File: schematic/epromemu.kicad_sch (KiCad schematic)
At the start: 10 parts, among them J1 EPROM Connector, U1 Teensy4.1, U2 74HC245, U3 74HC245, U4 74HC245, U5 74HC245

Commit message: v0.2 updates
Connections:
- net CE_3V3: now also U1.22 (30_CRX3); no longer U1.26 (34_RX8)
- net CE_5V: now also U2.19 (CE)
- net OE_5V: now also U5.11 (B7); no longer U2.19 (CE)
- net PGM_3V3: now also U1.20 (28_RX7), U3.11 (B7); no longer U1.25 (33_MCLK2), U5.9 (A7)
- net PGM_5V: now also U3.9 (A7); no longer U5.11 (B7)
- net OE_3V3: now reaches U1.23 (31_CTX3)
- net OE_3V3: now also U5.9 (A7)
- no-connect marks 26 -> 23
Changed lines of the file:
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@@
   (junction (at 71.12 123.19) (diameter 0) (color 0 0 0 0)
   )
-  (no_connect (at 107.95 82.55))
   (no_connect (at 107.95 39.37))
   (no_connect (at 107.95 54.61))
   (no_connect (at 163.83 31.75))
   (no_connect (at 107.95 80.01))
+  (no_connect (at 163.83 85.09))
   (no_connect (at 83.82 105.41))
   (no_connect (at 163.83 64.77))
@@
   (no_connect (at 58.42 100.33))
   (no_connect (at 107.95 87.63))
-  (no_connect (at 83.82 107.95))
   (no_connect (at 58.42 102.87))
   (no_connect (at 107.95 31.75))
@@
   (no_connect (at 83.82 102.87))
   (no_connect (at 83.82 100.33))
-  (no_connect (at 58.42 107.95))
+  (no_connect (at 163.83 87.63))
   (no_connect (at 107.95 44.45))
   (no_connect (at 58.42 105.41))
-  (no_connect (at 107.95 85.09))
-  (no_connect (at 107.95 77.47))
   (wire (pts (xy 58.42 113.03) (xy 46.99 113.03))
     (stroke (width 0) (type default) (color 0 0 0 0))
@@
     )
   )
-  (global_label "PGM_5V" (shape input) (at 212.09 107.95 0) (fields_autoplaced)
-    (effects (font (size 1.27 1.27)) (justify left))
-    (property "Intersheet References" "${INTERSHEET_REFS}" (id 0) (at 0 0 0)
-      (effects (font (size 1.27 1.27)) hide)
-    )
-  )
   (global_label "A1_3V3" (shape input) (at 186.69 49.53 180) (fields_autoplaced)
     (effects (font (size 1.27 1.27)) (justify right))
@@
     )
   )
-  (global_label "PGM_3V3" (shape input) (at 163.83 87.63 0) (fields_autoplaced)
-    (effects (font (size 1.27 1.27)) (justify left))
-    (property "Intersheet References" "${INTERSHEET_REFS}" (id 0) (at 0 0 0)
+  (global_label "PGM_3V3" (shape input) (at 107.95 77.47 180) (fields_autoplaced)
+    (effects (font (size 1.27 1.27)) (justify right))
+    (property "Intersheet References" "${INTERSHEET_REFS}" (id 0) (at 271.78 165.1 0)
       (effects (font (size 1.27 1.27)) hide)
     )
@@
     )
   )
-  (global_label "OE_5V" (shape input) (at 58.42 60.96 180) (fields_autoplaced)
-    (effects (font (size 1.27 1.27)) (justify right))
-    (property "Intersheet References" "${INTERSHEET_REFS}" (id 0) (at 0 0 0)
-      (effects (font (size 1.27 1.27)) hide)
+  (global_label "CE_5V" (shape input) (at 58.42 60.96 180) (fields_autoplaced)
+    (effects (font (size 1.27 1.27)) (justify right))
+    (property "Intersheet References" "${INTERSHEET_REFS}" (id 0) (at 50.411 60.8806 0)
+      (effects (font (size 1.27 1.27)) (justify right) hide)
     )
   )
@@
     )
   )
-  (global_label "CE_3V3" (shape input) (at 163.83 85.09 0) (fields_autoplaced)
-    (effects (font (size 1.27 1.27)) (justify left))
-    (property "Intersheet References" "${INTERSHEET_REFS}" (id 0) (at 0 0 0)
+  (global_label "CE_3V3" (shape input) (at 107.95 82.55 180) (fields_autoplaced)
+    (effects (font (size 1.27 1.27)) (justify right))
+    (property "Intersheet References" "${INTERSHEET_REFS}" (id 0) (at 271.78 167.64 0)
       (effects (font (size 1.27 1.27)) hide)
     )
@@
     )
   )
+  (global_label "OE_3V3" (shape input) (at 186.69 107.95 180) (fields_autoplaced)
+    (effects (font (size 1.27 1.27)) (justify right))
+    (property "Intersheet References" "${INTERSHEET_REFS}" (id 0) (at 177.411 107.8706 0)
+      (effects (font (size 1.27 1.27)) (justify right) hide)
+    )
+  )
   (global_label "A4_5V" (shape input) (at 212.09 97.79 0) (fields_autoplaced)
     (effects (font (size 1.27 1.27)) (justify left))
@@
     )
   )
+  (global_label "PGM_3V3" (shape input) (at 83.82 107.95 0) (fields_autoplaced)
+    (effects (font (size 1.27 1.27)) (justify left))
+    (property "Intersheet References" "${INTERSHEET_REFS}" (id 0) (at -80.01 20.32 0)
+      (effects (font (size 1.27 1.27)) hide)
+    )
+  )
   (global_label "A0_3V3" (shape input) (at 186.69 46.99 180) (fields_autoplaced)
     (effects (font (size 1.27 1.27)) (justify right))
@@
     )
   )
-  (global_label "PGM_3V3" (shape input) (at 186.69 107.95 180) (fields_autoplaced)
-    (effects (font (size 1.27 1.27)) (justify right))
-    (property "Intersheet References" "${INTERSHEET_REFS}" (id 0) (at 0 0 0)
-      (effects (font (size 1.27 1.27)) hide)
-    )
-  )
   (global_label "A12_3V3" (shape input) (at 186.69 102.87 180) (fields_autoplaced)
     (effects (font (size 1.27 1.27)) (justify right))
@@
     )
   )
+  (global_label "PGM_5V" (shape input) (at 58.42 107.95 180) (fields_autoplaced)
+    (effects (font (size 1.27 1.27)) (justify right))
+    (property "Intersheet References" "${INTERSHEET_REFS}" (id 0) (at 200.66 214.63 0)
+      (effects (font (size 1.27 1.27)) hide)
+    )
+  )
   (global_label "A11_5V" (shape input) (at 142.24 121.92 0) (fields_autoplaced)
     (effects (font (size 1.27 1.27)) (justify left))
@@
     )
   )
+  (global_label "OE_3V3" (shape input) (at 107.95 85.09 180) (fields_autoplaced)
+    (effects (font (size 1.27 1.27)) (justify right))
+    (property "Intersheet References" "${INTERSHEET_REFS}" (id 0) (at 98.671 85.0106 0)
+      (effects (font (size 1.27 1.27)) (justify right) hide)
+    )
+  )
   (global_label "A8_3V3" (shape input) (at 163.83 39.37 0) (fields_autoplaced)
     (effects (font (size 1.27 1.27)) (justify left))
@@
       (effects (font (size 1.27 1.27)) hide)
     )
+  )
+  (global_label "OE_5V" (shape input) (at 212.09 107.95 0) (fields_autoplaced)
+    (effects (font (size 1.27 1.27)) (justify left))
+    (property "Intersheet References" "${INTERSHEET_REFS}" (id 0) (at 69.85 -16.51 0)
+      (effects (font (size 1.27 1.27)) hide)
+    )

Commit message: v0.2 in progress...
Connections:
- net CE_3V3: now also U1.23 (31_CTX3), U3.11 (B7); no longer U1.22 (30_CRX3), U5.8 (A6)
- net CE_5V: now also U3.9 (A7); no longer U2.19 (CE), U5.12 (B6)
- net OE_3V3: now also U1.22 (30_CRX3), U3.12 (B6); no longer U1.23 (31_CTX3), U5.9 (A7)
- net OE_5V: now also U3.8 (A6); no longer U5.11 (B7)
- net CE_OE: now reaches U1.21 (29_TX7)
- net CE_OE: now also U2.19 (CE)
- net A18_3V3: now reaches U3.14 (B4)
- net A18_3V3: now also U1.20 (28_RX7)
- net A18_5V: now reaches U3.6 (A4)
- net A18_5V: now also J1.31 (Pin_31)
- removed net PGM_3V3: U1.20 (28_RX7), U3.11 (B7)
- removed net PGM_5V: J1.31 (Pin_31), U3.9 (A7)
- no-connect marks 23 -> 22

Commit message: v2 updates
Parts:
- added C6: 0.1uf, Capacitor_THT:C_Disc_D5.0mm_W2.5mm_P5.00mm, symbol Device:C_Small
- added U6: 74LS32, Package_DIP:DIP-14_W7.62mm_Socket, symbol 74xx:74LS32
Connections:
- net +5V: now also C6.1, U6.14 (VCC)
- net CE_5V: now also U6.2; no longer U3.9 (A7)
- net GND: now also C6.2, U6.10, U6.11, U6.12, U6.13, U6.4, U6.5, U6.6, U6.7 (GND), U6.8, U6.9
- net OE_5V: now also U6.1; no longer U3.8 (A6)
- net CE_3V3: no longer names the net of U1.23 (31_CTX3)
- net CE_3V3: no longer U3.11 (B7)
- net CE_OE: no longer names the net of U1.21 (29_TX7)
- net CE_OE: no longer U2.19 (CE)
- net OE_3V3: no longer names the net of U1.22 (30_CRX3)
- net OE_3V3: no longer U3.12 (B6)
- new net: U2.19 (CE), U6.3
- no-connect marks 22 -> 29

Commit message: starting v0.3
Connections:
- net +5V: now also U1.48 (VIN); no longer J1.1 (Pin_1)
- net A14_3V3: now also U3.14 (B4); no longer U3.16 (B2)
- net A14_5V: now also U3.6 (A4); no longer U3.4 (A2)
- net A15_3V3: now also U3.13 (B5); no longer U3.15 (B3)
- net A15_5V: now also U3.7 (A5); no longer U3.5 (A3)
- net A16_3V3: now also U3.16 (B2); no longer U3.18 (B0)
- net A16_5V: now also U3.4 (A2); no longer U3.2 (A0)
- net A17_3V3: now also U3.15 (B3); no longer U3.17 (B1)
- net A17_5V: now also U3.5 (A3); no longer U3.3 (A1)
- net A18_3V3: now also U1.3 (1_TX1_CTX2_MISO1), U3.17 (B1); no longer U1.20 (28_RX7), U3.14 (B4)
- net A18_5V: now also U3.3 (A1); no longer U3.6 (A4)
- net A19_3V3: now reaches U1.2 (0_RX1_CRX2_CS1)
- net A19_3V3: now also U3.18 (B0)
- new net A19_5V: J1.1 (Pin_1), U3.2 (A0)
- no-connect marks 29 -> 24

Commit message: a complete v3?
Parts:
- added JP1: PWR, Connector_PinHeader_2.54mm:PinHeader_1x02_P2.54mm_Vertical, symbol Jumper:Jumper_2_Open
- U6: value 74LS32 -> 74HC32
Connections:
- net +5V: now also JP1.2 (B); no longer J1.32 (Pin_32)
- net A14_3V3: now also U3.15 (B3); no longer U3.14 (B4)
- net A14_5V: now also U3.5 (A3); no longer U3.6 (A4)
- net A15_3V3: now also U3.14 (B4); no longer U3.13 (B5)
- net A15_5V: now also U3.6 (A4); no longer U3.7 (A5)
- net A16_3V3: now also U1.4 (2_OUT2), U3.18 (B0); no longer U1.16 (24_A10_TX6_SCL2), U3.16 (B2)
- net A16_5V: now also U3.2 (A0); no longer U3.4 (A2)
- net A17_3V3: now also U1.5 (3_LRCLK2), U3.17 (B1); no longer U1.17 (25_A11_RX6_SDA2), U3.15 (B3)
- net A17_5V: now also U3.3 (A1); no longer U3.5 (A3)
- net A18_3V3: now also U1.6 (4_BCLK2), U3.16 (B2); no longer U1.3 (1_TX1_CTX2_MISO1), U3.17 (B1)
- net A18_5V: now also U3.4 (A2); no longer U3.3 (A1)
- net A19_3V3: now also U1.25 (33_MCLK2), U5.8 (A6); no longer U1.2 (0_RX1_CRX2_CS1), U3.18 (B0)
- net A19_5V: now also U5.12 (B6); no longer U3.2 (A0)
- net GND: no longer U6.11, U6.6, U6.8
- new net: J1.32 (Pin_32), JP1.1 (A)
- no-connect marks 24 -> 47
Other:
- moved on the sheet: J1

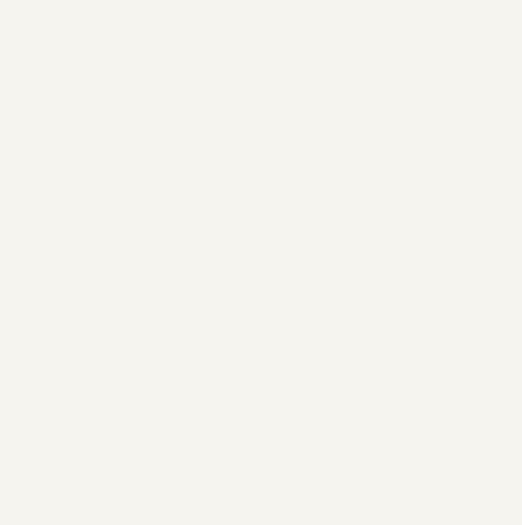
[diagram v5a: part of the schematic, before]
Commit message: mounting holes
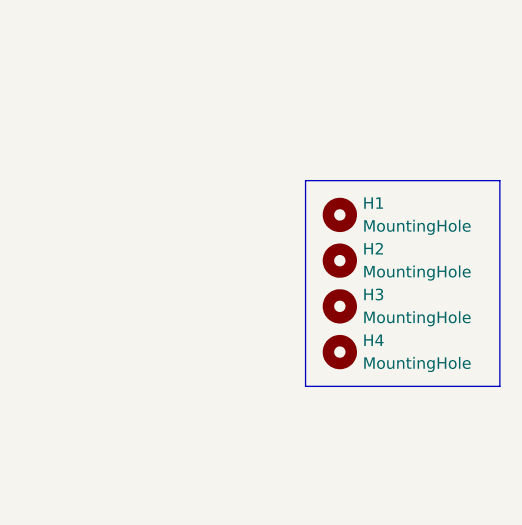
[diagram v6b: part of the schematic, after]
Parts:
- added H1, H2, H3, H4: MountingHole, MountingHole:MountingHole_2.2mm_M2_ISO7380_Pad, symbol Mechanical:MountingHole
